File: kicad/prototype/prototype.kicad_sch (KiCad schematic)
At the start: 7 parts, among them U1 Pico

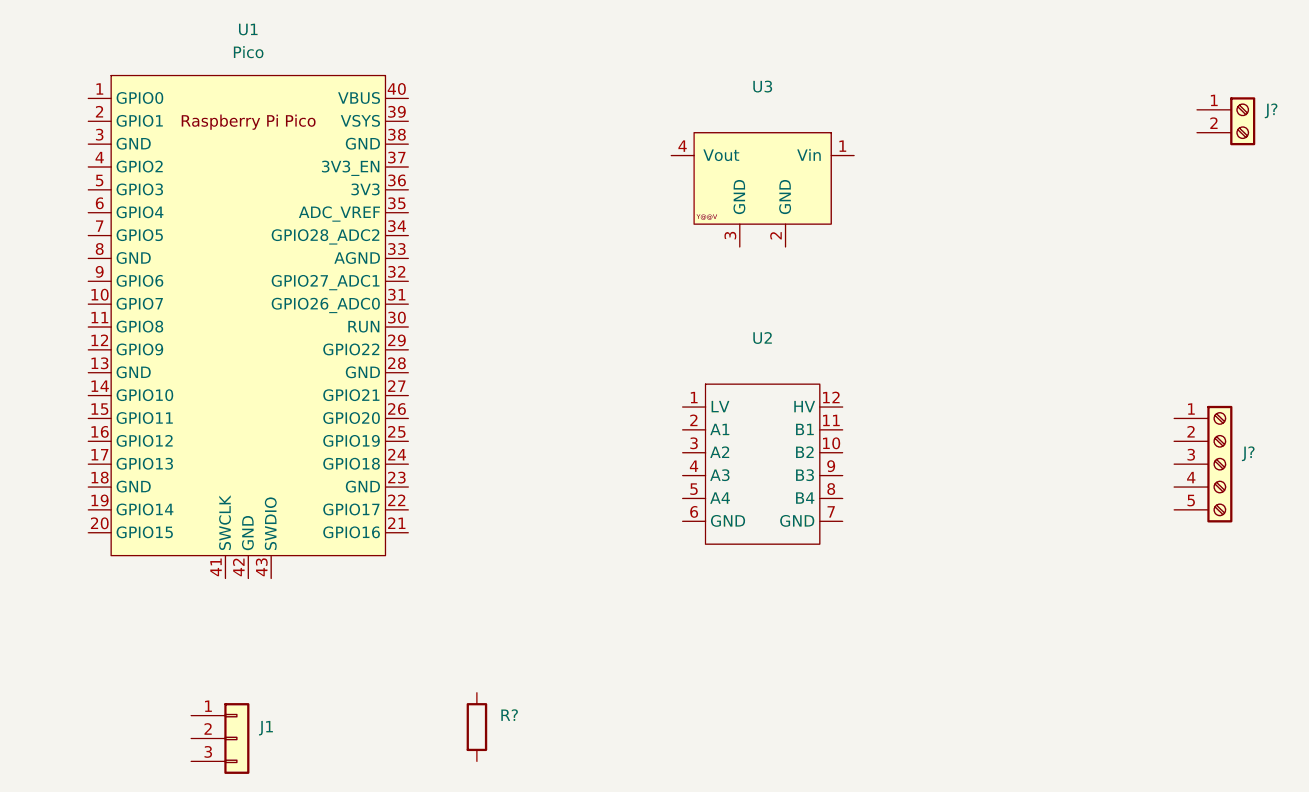
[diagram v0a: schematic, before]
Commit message: Updated schematics with HID LED
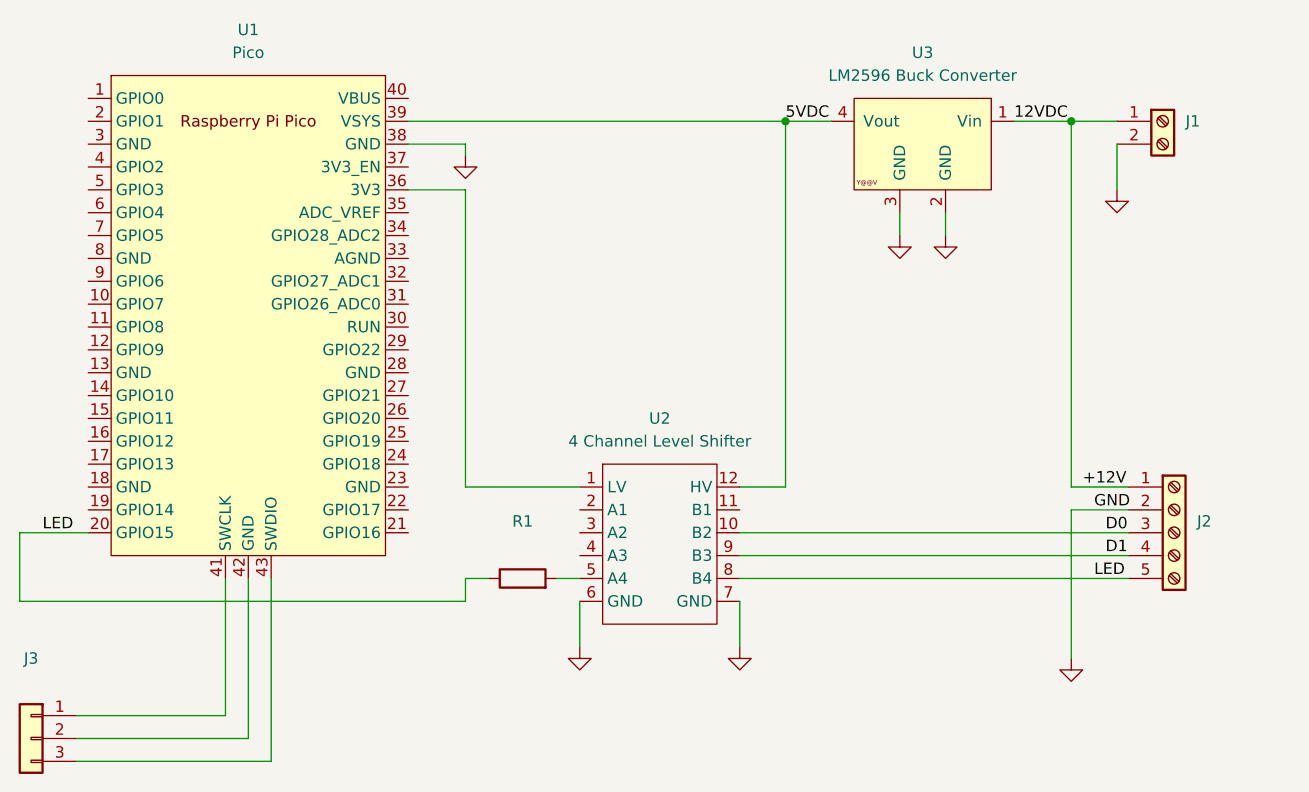
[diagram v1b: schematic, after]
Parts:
- U2: value (none) -> 4 Channel Level Shifter
- U3: value (none) -> LM2596 Buck Converter
- gave numbers to parts that had none: 3
- renumbered J1 to J3
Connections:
- net +12V: now reaches U3.1 (Vin)
- net +12V: now also J1.1 (Pin_1), J2.1 (Pin_1)
- net GND: now reaches U3.2 (GND)
- net GND: now also J1.2 (Pin_2), J2.2 (Pin_2), U1.38 (GND), U2.6 (GND), U2.7 (GND), U3.3 (GND)
- net 5VDC: now reaches U3.4 (Vout)
- net 5VDC: now also U1.39 (VSYS), U2.12 (HV)
- net at J3.1 (Pin_1): now also U1.41 (SWCLK)
- net at J3.2 (Pin_2): now also U1.42 (GND)
- net at J3.3 (Pin_3): now also U1.43 (SWDIO)
- net LED: now reaches R1.1
- net LED: now also J2.5 (Pin_5), U1.20 (GPIO15), U2.8 (B4)
- net at R1.2: now also U2.5 (A4)
- net at U2.1 (LV): now also U1.36 (3V3)
- net D0: now reaches U2.10 (B2)
- net D0: now also J2.3 (Pin_3)
- net D1: now reaches U2.9 (B3)
- net D1: now also J2.4 (Pin_4)
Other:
- moved on the sheet: J1, J2, J3, R1, U2, U3
